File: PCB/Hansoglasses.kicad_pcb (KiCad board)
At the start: 4 copper layers, 56.5 x 27 mm, 24 parts, among them J1 Conn_01x02_Pin, J11 USB_C_Receptacle_USB2.0_16P, J2 Conn_01x02_Pin, J3 Conn_01x02_Pin, J4 Conn_01x02_Pin, SW1 SW_SPDT, U1 ESP32-S3-WROOM-1, U2 MAX98357A, U3 MAX98357A, U4 RT9013-33GB

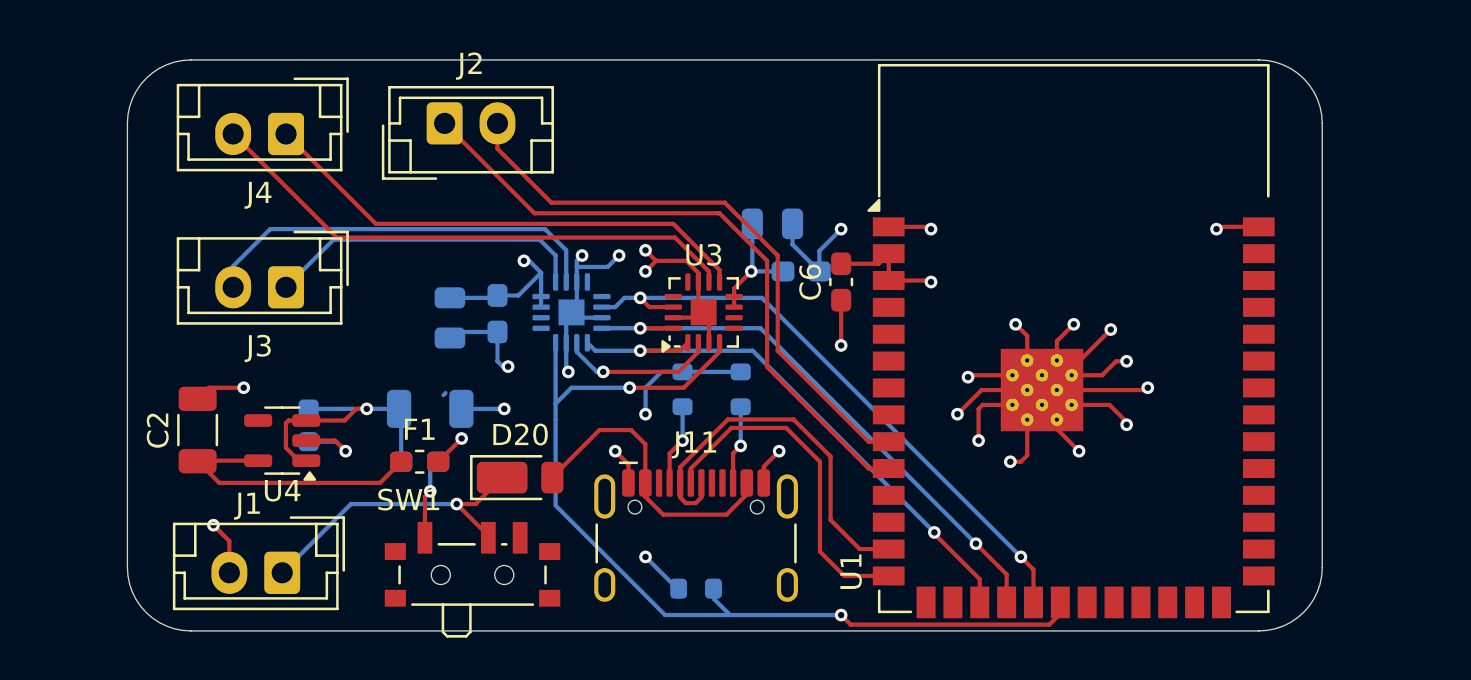
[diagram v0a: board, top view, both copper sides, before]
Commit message: horizontal layout ver
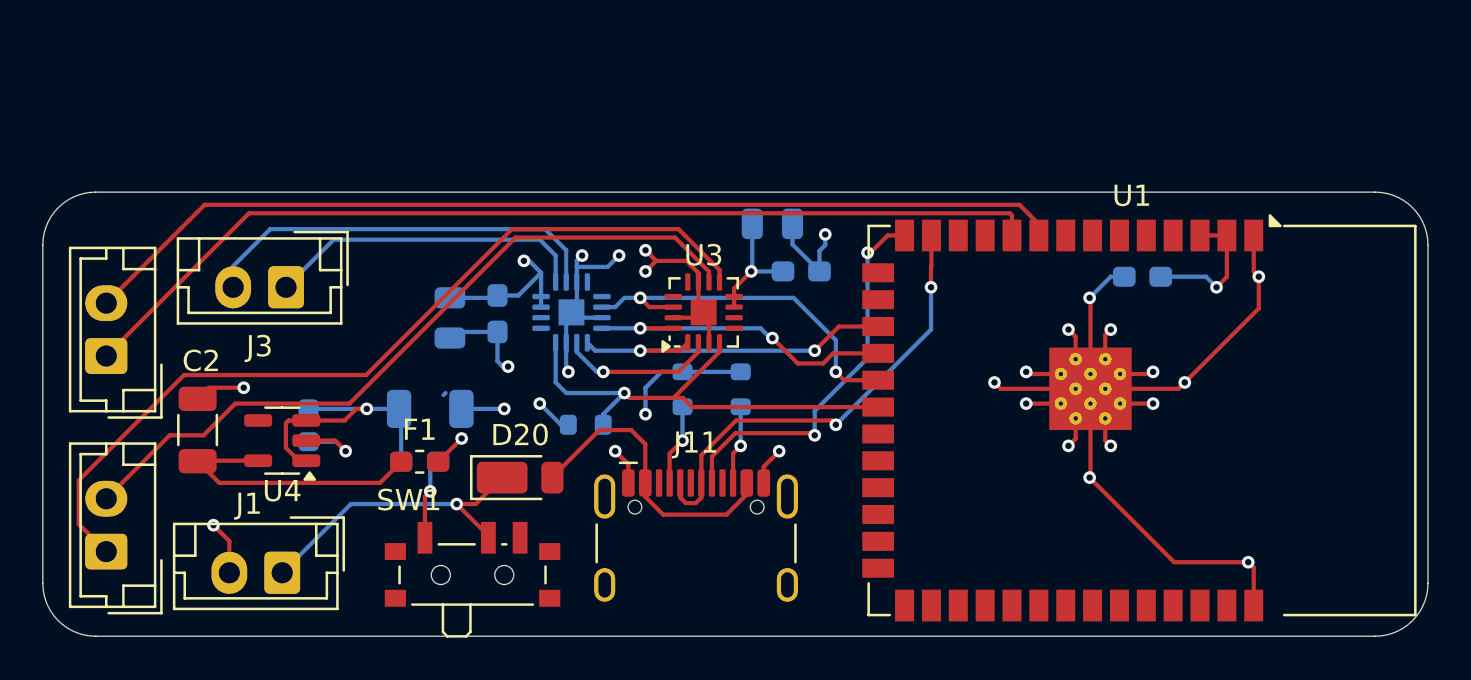
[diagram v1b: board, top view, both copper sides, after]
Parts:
- C6: moved to B.Cu
- moved J4 21.5 mm to (169.5, 58.5), turned to 90 degrees
- moved J2 19.4 mm to (169.5, 49.2), turned to 90 degrees
- moved C6 14.3 mm to (218.5, 45.5), turned to 0 degrees
- moved R9 9.34 mm to (192.2, 52.5)
- moved U1 5.08 mm to (218.5, 52.3), turned to -90 degrees
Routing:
- net /MCU/SD_MODE: track 45.4 -> 23.0 mm, vias 2 -> 1
- net /Connectors/RX_PICO: track 28.1 -> 46.9 mm
- net /Connectors/OUTP_2: track 23.7 -> 40.5 mm
- net /Connectors/TX_PICO: track 30.7 -> 46.6 mm
- net /MCU/I2S_LRCLK: track 29.2 -> 17.5 mm
- net /MCU/I2S_BCLK: track 26.8 -> 15.5 mm
- net GND: track 87.7 -> 98.1 mm
- net /MCU/I2S_DOUT: track 26.7 -> 16.8 mm
- net /Connectors/OUTN_2: track 25.7 -> 34.8 mm
- net /MCU/USB_DN: track 18.4 -> 21.8 mm, vias 0 -> 2
- net /MCU/USB_DP: track 16.2 -> 18.4 mm, vias 0 -> 2
- net +3V3: track 30.4 -> 31.0 mm
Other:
- board size 56.5 x 27 mm -> 65.5 x 21 mm

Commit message: horiz layout changes
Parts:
- added G***: LOGO, YerraGlasses:mv3, B.Cu at (211.0, 53.0)
- added G***: LOGO, YerraGlasses:alejandro, B.Cu at (224.4, 53.0)
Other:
- board size 65.5 x 21 mm -> 65.5 x 21.5 mm
